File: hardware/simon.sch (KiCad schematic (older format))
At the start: 18 parts, among them SW0 SW_RED, SW1 SW_YELLOW, SW2 SW_GREEN, SW3 SW_BLUE

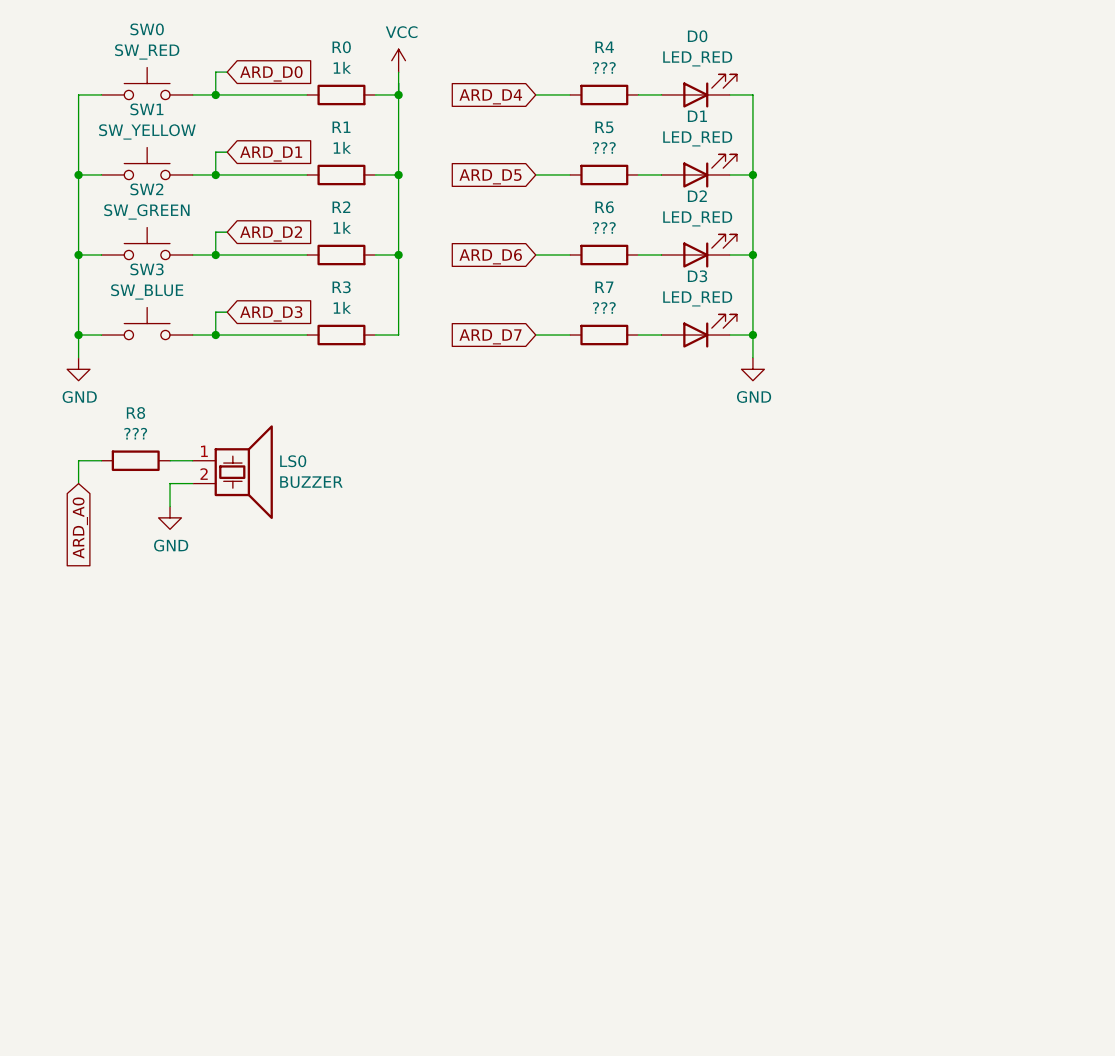
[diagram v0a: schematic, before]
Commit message: updated resistor values in hardware schematics
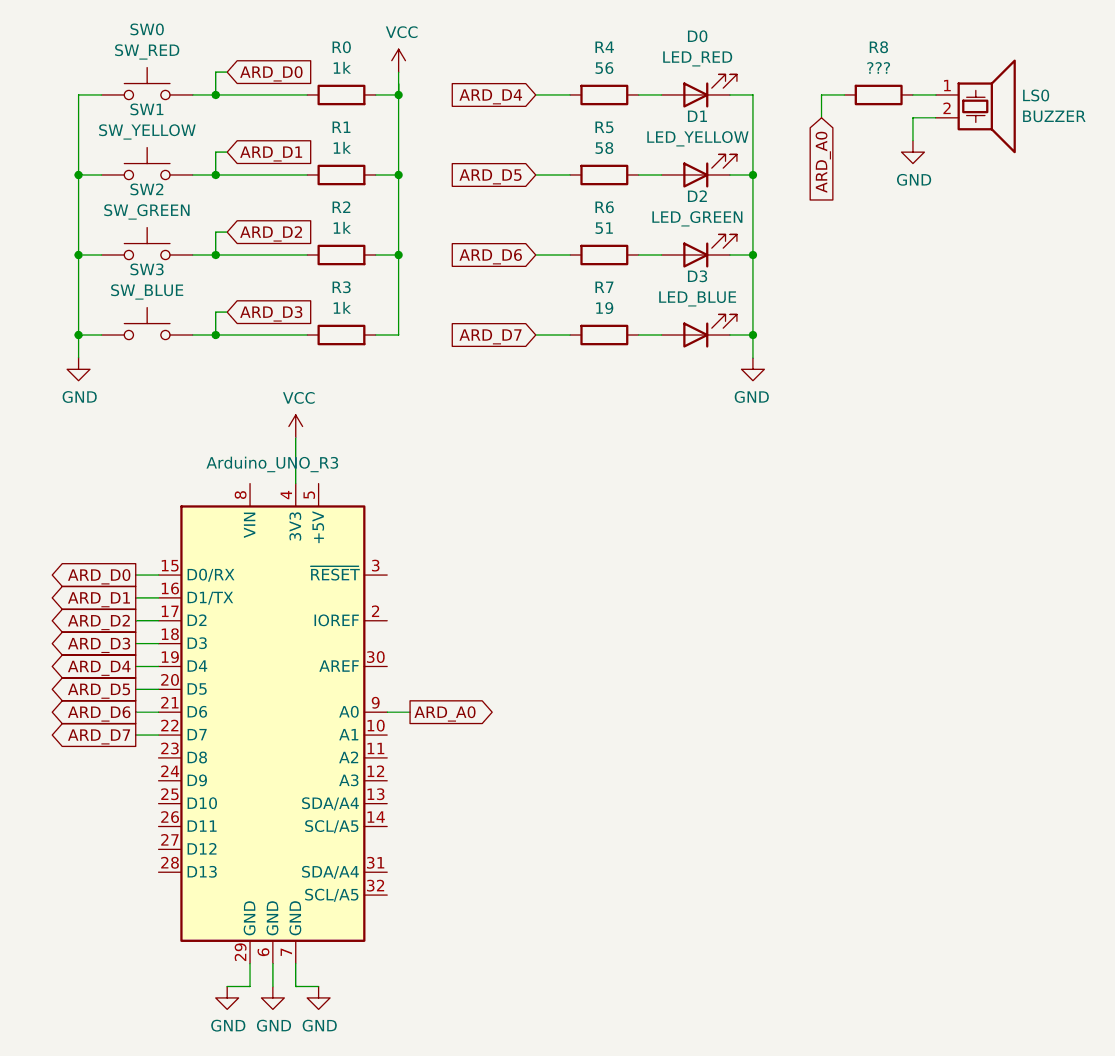
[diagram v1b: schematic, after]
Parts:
- added A0: Arduino_UNO_R3, Module:Arduino_UNO_R3, symbol MCU_Module:Arduino_UNO_R3
- D0: footprint (none) -> LED_THT:LED_D3.0mm
- D1: value LED_RED -> LED_YELLOW; footprint (none) -> LED_THT:LED_D3.0mm
- D2: value LED_RED -> LED_GREEN; footprint (none) -> LED_THT:LED_D3.0mm
- D3: value LED_RED -> LED_BLUE; footprint (none) -> LED_THT:LED_D3.0mm
- LS0: footprint (none) -> Buzzer_Beeper:Buzzer_12x9.5RM7.6
- R0, R1, R2, R3, R8: footprint (none) -> Resistor_THT:R_Axial_DIN0207_L6.3mm_D2.5mm_P10.16mm_Horizontal
- R4: value ??? -> 56; footprint (none) -> Resistor_THT:R_Axial_DIN0207_L6.3mm_D2.5mm_P10.16mm_Horizontal
- R5: value ??? -> 58; footprint (none) -> Resistor_THT:R_Axial_DIN0207_L6.3mm_D2.5mm_P10.16mm_Horizontal
- R6: value ??? -> 51; footprint (none) -> Resistor_THT:R_Axial_DIN0207_L6.3mm_D2.5mm_P10.16mm_Horizontal
- R7: value ??? -> 19; footprint (none) -> Resistor_THT:R_Axial_DIN0207_L6.3mm_D2.5mm_P10.16mm_Horizontal
- SW0, SW1, SW2, SW3: footprint (none) -> Button_Switch_THT:SW_PUSH_6mm_H4.3mm
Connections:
- net ARD_A0: now also A0.9 (A0)
- net ARD_D0: now also A0.15 (D0/RX)
- net ARD_D1: now also A0.16 (D1/TX)
- net ARD_D2: now also A0.17 (D2)
- net ARD_D3: now also A0.18 (D3)
- net ARD_D4: now also A0.19 (D4)
- net ARD_D5: now also A0.20 (D5)
- net ARD_D6: now also A0.21 (D6)
- net ARD_D7: now also A0.22 (D7)
- net GND: now also A0.29 (GND), A0.6 (GND), A0.7 (GND)
- net VCC: now also A0.4 (3V3)
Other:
- moved on the sheet: LS0, R8
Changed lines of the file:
@@
 $EndDescr
 $Comp
-L power:GND #PWR?
+L power:GND #PWR0101
 U 1 1 617FA64B
 P 650 2000
-F 0 "#PWR?" H 650 1750 50  0001 C CNN
+F 0 "#PWR0101" H 650 1750 50  0001 C CNN
 F 1 "GND" H 655 1827 50  0000 C CNN
 F 2 "" H 650 2000 50  0001 C CNN
@@
 $EndComp
 $Comp
-L power:VCC #PWR?
+L power:VCC #PWR0102
 U 1 1 617FAA56
 P 2050 750
-F 0 "#PWR?" H 2050 600 50  0001 C CNN
+F 0 "#PWR0102" H 2050 600 50  0001 C CNN
 F 1 "VCC" H 2065 923 50  0000 C CNN
 F 2 "" H 2050 750 50  0001 C CNN
@@
 F 0 "SW0" H 950 1135 50  0000 C CNN
 F 1 "SW_RED" H 950 1044 50  0000 C CNN
-F 2 "" H 950 1050 50  0001 C CNN
+F 2 "Button_Switch_THT:SW_PUSH_6mm_H4.3mm" H 950 1050 50  0001 C CNN
 F 3 "~" H 950 1050 50  0001 C CNN
 	1    950  850
@@
 F 0 "SW1" H 950 1485 50  0000 C CNN
 F 1 "SW_YELLOW" H 950 1394 50  0000 C CNN
-F 2 "" H 950 1400 50  0001 C CNN
+F 2 "Button_Switch_THT:SW_PUSH_6mm_H4.3mm" H 950 1400 50  0001 C CNN
 F 3 "~" H 950 1400 50  0001 C CNN
 	1    950  1200
@@
 F 0 "SW2" H 950 1835 50  0000 C CNN
 F 1 "SW_GREEN" H 950 1744 50  0000 C CNN
-F 2 "" H 950 1750 50  0001 C CNN
+F 2 "Button_Switch_THT:SW_PUSH_6mm_H4.3mm" H 950 1750 50  0001 C CNN
 F 3 "~" H 950 1750 50  0001 C CNN
 	1    950  1550
@@
 F 0 "SW3" H 950 2185 50  0000 C CNN
 F 1 "SW_BLUE" H 950 2094 50  0000 C CNN
-F 2 "" H 950 2100 50  0001 C CNN
+F 2 "Button_Switch_THT:SW_PUSH_6mm_H4.3mm" H 950 2100 50  0001 C CNN
 F 3 "~" H 950 2100 50  0001 C CNN
 	1    950  1900
@@
 F 0 "R3" V 2007 1900 50  0000 C CNN
 F 1 "1k" V 1916 1900 50  0000 C CNN
-F 2 "" V 1730 1900 50  0001 C CNN
+F 2 "Resistor_THT:R_Axial_DIN0207_L6.3mm_D2.5mm_P10.16mm_Horizontal" V 1730 1900 50  0001 C CNN
 F 3 "~" H 1800 1900 50  0001 C CNN
 	1    1800 1900
@@
 F 0 "R2" V 2007 1550 50  0000 C CNN
 F 1 "1k" V 1916 1550 50  0000 C CNN
-F 2 "" V 1730 1550 50  0001 C CNN
+F 2 "Resistor_THT:R_Axial_DIN0207_L6.3mm_D2.5mm_P10.16mm_Horizontal" V 1730 1550 50  0001 C CNN
 F 3 "~" H 1800 1550 50  0001 C CNN
 	1    1800 1550
@@
 F 0 "R1" V 2007 1200 50  0000 C CNN
 F 1 "1k" V 1916 1200 50  0000 C CNN
-F 2 "" V 1730 1200 50  0001 C CNN
+F 2 "Resistor_THT:R_Axial_DIN0207_L6.3mm_D2.5mm_P10.16mm_Horizontal" V 1730 1200 50  0001 C CNN
 F 3 "~" H 1800 1200 50  0001 C CNN
 	1    1800 1200
@@
 F 0 "R0" V 2007 850 50  0000 C CNN
 F 1 "1k" V 1916 850 50  0000 C CNN
-F 2 "" V 1730 850 50  0001 C CNN
+F 2 "Resistor_THT:R_Axial_DIN0207_L6.3mm_D2.5mm_P10.16mm_Horizontal" V 1730 850 50  0001 C CNN
 F 3 "~" H 1800 850 50  0001 C CNN
 	1    1800 850
@@
 P 2950 850
 F 0 "R4" V 2743 850 50  0000 C CNN
-F 1 "???" V 2834 850 50  0000 C CNN
-F 2 "" V 2880 850 50  0001 C CNN
+F 1 "56" V 2834 850 50  0000 C CNN
+F 2 "Resistor_THT:R_Axial_DIN0207_L6.3mm_D2.5mm_P10.16mm_Horizontal" V 2880 850 50  0001 C CNN
 F 3 "~" H 2950 850 50  0001 C CNN
 	1    2950 850
@@
 P 2950 1200
 F 0 "R5" V 2743 1200 50  0000 C CNN
-F 1 "???" V 2834 1200 50  0000 C CNN
-F 2 "" V 2880 1200 50  0001 C CNN
+F 1 "58" V 2834 1200 50  0000 C CNN
+F 2 "Resistor_THT:R_Axial_DIN0207_L6.3mm_D2.5mm_P10.16mm_Horizontal" V 2880 1200 50  0001 C CNN
 F 3 "~" H 2950 1200 50  0001 C CNN
 	1    2950 1200
@@
 P 2950 1550
 F 0 "R6" V 2743 1550 50  0000 C CNN
-F 1 "???" V 2834 1550 50  0000 C CNN
-F 2 "" V 2880 1550 50  0001 C CNN
+F 1 "51" V 2834 1550 50  0000 C CNN
+F 2 "Resistor_THT:R_Axial_DIN0207_L6.3mm_D2.5mm_P10.16mm_Horizontal" V 2880 1550 50  0001 C CNN
 F 3 "~" H 2950 1550 50  0001 C CNN
 	1    2950 1550
@@
 P 2950 1900
 F 0 "R7" V 2743 1900 50  0000 C CNN
-F 1 "???" V 2834 1900 50  0000 C CNN
-F 2 "" V 2880 1900 50  0001 C CNN
+F 1 "19" V 2834 1900 50  0000 C CNN
+F 2 "Resistor_THT:R_Axial_DIN0207_L6.3mm_D2.5mm_P10.16mm_Horizontal" V 2880 1900 50  0001 C CNN
 F 3 "~" H 2950 1900 50  0001 C CNN
 	1    2950 1900
@@
 	2650 1900 2800 1900
 $Comp
-L power:GND #PWR?
+L power:GND #PWR0103
 U 1 1 61831AB4
 P 3600 2000
-F 0 "#PWR?" H 3600 1750 50  0001 C CNN
+F 0 "#PWR0103" H 3600 1750 50  0001 C CNN
 F 1 "GND" H 3605 1827 50  0000 C CNN
 F 2 "" H 3600 2000 50  0001 C CNN
 F 3 "" H 3600 2000 50  0001 C CNN
 	1    3600 2000
-	1    0    0    -1
+	-1   0    0    -1
 $EndComp
 $Comp
@@
 F 0 "D0" H 3343 595 50  0000 C CNN
 F 1 "LED_RED" H 3343 686 50  0000 C CNN
-F 2 "" H 3350 850 50  0001 C CNN
+F 2 "LED_THT:LED_D3.0mm" H 3350 850 50  0001 C CNN
 F 3 "~" H 3350 850 50  0001 C CNN
 	1    3350 850
@@
 P 3350 1200
 F 0 "D1" H 3343 945 50  0000 C CNN
-F 1 "LED_RED" H 3343 1036 50  0000 C CNN
-F 2 "" H 3350 1200 50  0001 C CNN
+F 1 "LED_YELLOW" H 3343 1036 50  0000 C CNN
+F 2 "LED_THT:LED_D3.0mm" H 3350 1200 50  0001 C CNN
 F 3 "~" H 3350 1200 50  0001 C CNN
 	1    3350 1200
@@
 P 3350 1550
 F 0 "D2" H 3343 1295 50  0000 C CNN
-F 1 "LED_RED" H 3343 1386 50  0000 C CNN
-F 2 "" H 3350 1550 50  0001 C CNN
+F 1 "LED_GREEN" H 3343 1386 50  0000 C CNN
+F 2 "LED_THT:LED_D3.0mm" H 3350 1550 50  0001 C CNN
 F 3 "~" H 3350 1550 50  0001 C CNN
 	1    3350 1550
@@
 P 3350 1900
 F 0 "D3" H 3343 1645 50  0000 C CNN
-F 1 "LED_RED" H 3343 1736 50  0000 C CNN
-F 2 "" H 3350 1900 50  0001 C CNN
+F 1 "LED_BLUE" H 3343 1736 50  0000 C CNN
+F 2 "LED_THT:LED_D3.0mm" H 3350 1900 50  0001 C CNN
 F 3 "~" H 3350 1900 50  0001 C CNN
 	1    3350 1900
@@
 L Device:Speaker_Crystal LS0
 U 1 1 618756C2
-P 1350 2450
-F 0 "LS0" H 1525 2446 50  0000 L CNN
-F 1 "BUZZER" H 1525 2355 50  0000 L CNN
-F 2 "" H 1315 2400 50  0001 C CNN
-F 3 "~" H 1315 2400 50  0001 C CNN
-	1    1350 2450
+P 4600 850
+F 0 "LS0" H 4775 846 50  0000 L CNN
+F 1 "BUZZER" H 4775 755 50  0000 L CNN
+F 2 "Buzzer_Beeper:Buzzer_12x9.5RM7.6" H 4565 800 50  0001 C CNN
+F 3 "~" H 4565 800 50  0001 C CNN
+	1    4600 850
 	1    0    0    -1
 $EndComp
@@
 L Device:R R8
 U 1 1 61876E39
-P 900 2450
-F 0 "R8" V 693 2450 50  0000 C CNN
-F 1 "???" V 784 2450 50  0000 C CNN
-F 2 "" V 830 2450 50  0001 C CNN
-F 3 "~" H 900 2450 50  0001 C CNN
-	1    900  2450
+P 4150 850
+F 0 "R8" V 3943 850 50  0000 C CNN
+F 1 "???" V 4034 850 50  0000 C CNN
+F 2 "Resistor_THT:R_Axial_DIN0207_L6.3mm_D2.5mm_P10.16mm_Horizontal" V 4080 850 50  0001 C CNN
+F 3 "~" H 4150 850 50  0001 C CNN
+	1    4150 850
 	0    1    1    0
 $EndComp
 Wire Wire Line
-	1050 2450 1150 2450
-Text GLabel 650  2550 3    50   Input ~ 0
+	4300 850  4400 850
+Text GLabel 3900 950  3    50   Input ~ 0
 ARD_A0
 $Comp
-L power:GND #PWR?
+L power:GND #PWR0104
 U 1 1 6187DA46
-P 1050 2650
-F 0 "#PWR?" H 1050 2400 50  0001 C CNN
-F 1 "GND" H 1055 2477 50  0000 C CNN
-F 2 "" H 1050 2650 50  0001 C CNN
-F 3 "" H 1050 2650 50  0001 C CNN
-	1    1050 2650
-	1    0    0    -1
-$EndComp
-Wire Wire Line
-	1050 2650 1050 2550
-Wire Wire Line
-	1050 2550 1150 2550
-Wire Wire Line
-	750  2450 650  2450
-Wire Wire Line
-	650  2450 650  2550
+P 4300 1050
+F 0 "#PWR0104" H 4300 800 50  0001 C CNN
+F 1 "GND" H 4305 877 50  0000 C CNN
+F 2 "" H 4300 1050 50  0001 C CNN
+F 3 "" H 4300 1050 50  0001 C CNN
+	1    4300 1050
+	1    0    0    -1
+$EndComp
+Wire Wire Line
+	4300 1050 4300 950
+Wire Wire Line
+	4300 950  4400 950
+Wire Wire Line
+	4000 850  3900 850
+Wire Wire Line
+	3900 850  3900 950
+Text GLabel 900  2950 0    50   Output ~ 0
+ARD_D0
+Text GLabel 900  3050 0    50   Output ~ 0
+ARD_D1
+Text GLabel 900  3150 0    50   Output ~ 0
+ARD_D2
+Text GLabel 900  3250 0    50   Output ~ 0
+ARD_D3
+Text GLabel 900  3350 0    50   Output ~ 0
+ARD_D4
+Text GLabel 900  3450 0    50   Output ~ 0
+ARD_D5
+Text GLabel 900  3550 0    50   Output ~ 0
+ARD_D6
+Text GLabel 900  3650 0    50   Output ~ 0
+ARD_D7
+Wire Wire Line
+	1000 2950 900  2950
+Wire Wire Line
+	900  3050 1000 3050
+Wire Wire Line
+	1000 3150 900  3150
+Wire Wire Line
+	900  3250 1000 3250
+Wire Wire Line
+	1000 3350 900  3350
+Wire Wire Line
+	900  3450 1000 3450
+Wire Wire Line
+	1000 3550 900  3550
+Wire Wire Line
+	900  3650 1000 3650
+Text GLabel 2100 3550 2    50   Output ~ 0
+ARD_A0
+Wire Wire Line
+	2100 3550 2000 3550
+$Comp
+L MCU_Module:Arduino_UNO_R3 A0
+U 1 1 618123D3
+P 1500 3550
+F 0 "A0" H 1500 4731 50  0001 C CNN
+F 1 "Arduino_UNO_R3" H 1500 4639 50  0000 C CNN
+F 2 "Module:Arduino_UNO_R3" H 1500 3550 50  0001 C CIN
+F 3 "https://www.arduino.cc/en/Main/arduinoBoardUno" H 1500 3550 50  0001 C CNN
+	1    1500 3550
+	1    0    0    -1
+$EndComp
+$Comp
+L power:VCC #PWR0105
+U 1 1 61834727
+P 1600 2350
+F 0 "#PWR0105" H 1600 2200 50  0001 C CNN
+F 1 "VCC" H 1615 2523 50  0000 C CNN
+F 2 "" H 1600 2350 50  0001 C CNN
+F 3 "" H 1600 2350 50  0001 C CNN
+	1    1600 2350
+	1    0    0    -1
+$EndComp
+Wire Wire Line
+	1600 2350 1600 2550
+$Comp
+L power:GND #PWR0106
+U 1 1 61836617
+P 1700 4750
+F 0 "#PWR0106" H 1700 4500 50  0001 C CNN
+F 1 "GND" H 1705 4577 50  0000 C CNN
+F 2 "" H 1700 4750 50  0001 C CNN
+F 3 "" H 1700 4750 50  0001 C CNN
+	1    1700 4750
+	1    0    0    -1
+$EndComp
+Wire Wire Line
+	1600 4750 1600 4650
+$Comp
+L power:GND #PWR0107
+U 1 1 6180680E
+P 1500 4750
+F 0 "#PWR0107" H 1500 4500 50  0001 C CNN
+F 1 "GND" H 1505 4577 50  0000 C CNN
+F 2 "" H 1500 4750 50  0001 C CNN
+F 3 "" H 1500 4750 50  0001 C CNN
+	1    1500 4750
+	1    0    0    -1
+$EndComp
+Wire Wire Line
+	1500 4750 1500 4650
+$Comp
+L power:GND #PWR0108
+U 1 1 61807C2A
+P 1300 4750
+F 0 "#PWR0108" H 1300 4500 50  0001 C CNN
+F 1 "GND" H 1305 4577 50  0000 C CNN
+F 2 "" H 1300 4750 50  0001 C CNN
+F 3 "" H 1300 4750 50  0001 C CNN
+	1    1300 4750
+	1    0    0    -1
+$EndComp
+Wire Wire Line
+	1400 4750 1400 4650
+Wire Wire Line
+	1400 4750 1300 4750
+Wire Wire Line
+	1600 4750 1700 4750
 $EndSCHEMATC

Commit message: hardware schematics done, test code included
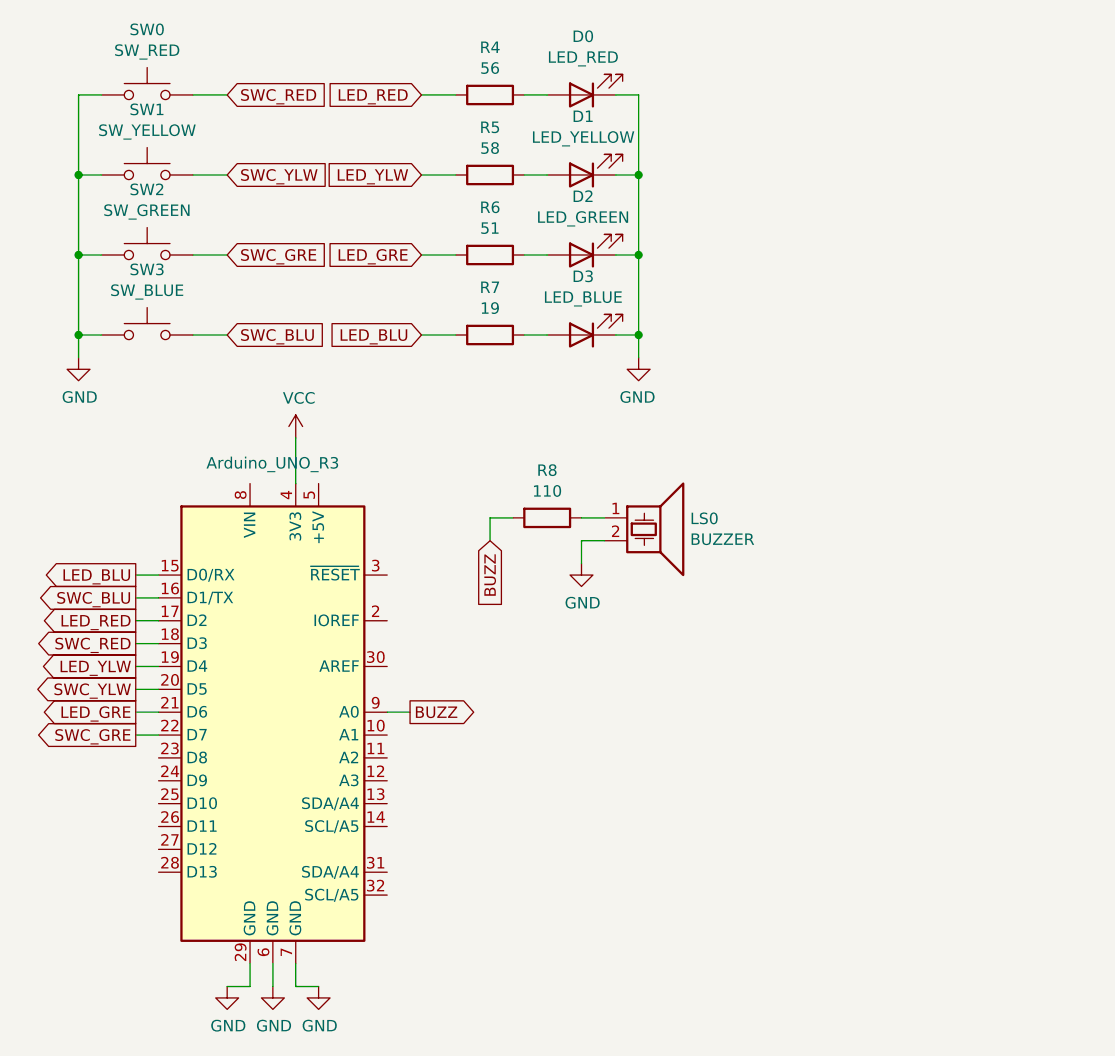
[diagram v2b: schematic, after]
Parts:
- removed R0, R1, R2, R3: 1k, Resistor_THT:R_Axial_DIN0207_L6.3mm_D2.5mm_P10.16mm_Horizontal, symbol Device:R
- R8: value ??? -> 110
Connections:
- net ARD_A0 renamed BUZZ
- net ARD_D0 renamed LED_BLU
- net LED_BLU: now also R7.2; no longer SW0.2
- net ARD_D1 renamed SWC_BLU
- net SWC_BLU: now also SW3.2; no longer SW1.2
- net ARD_D2 renamed LED_RED
- net LED_RED: now also R4.2; no longer SW2.2
- net ARD_D3 renamed SWC_RED
- net SWC_RED: now also SW0.2; no longer SW3.2
- net ARD_D4 renamed LED_YLW
- net LED_YLW: now also R5.2; no longer R4.2
- net ARD_D5 renamed SWC_YLW
- net SWC_YLW: now also SW1.2; no longer R5.2
- net ARD_D6 renamed LED_GRE
- net ARD_D7 renamed SWC_GRE
- net SWC_GRE: now also SW2.2; no longer R7.2
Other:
- moved on the sheet: D0, D1, D2, D3, LS0, R4, R5, R6, R7, R8
